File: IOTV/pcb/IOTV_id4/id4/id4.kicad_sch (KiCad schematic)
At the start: 7 parts, among them J1 Conn_01x04, J2 Conn_01x03, U1 WeMos_D1_mini

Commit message: pcb id4
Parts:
- removed D1, D2, D3, D4: LED, LED_THT:LED_D2.0mm_W4.8mm_H2.5mm_FlatTop, symbol Device:LED
- removed J1: Conn_01x04, Jumper:tht_jumper_x4-2.54mm, symbol PCM_4ms_Connector:Conn_01x04
- removed J2: Conn_01x03, Jumper:tht_jumper_x3-2.54mm, symbol PCM_4ms_Connector:Conn_01x03
- removed U1: WeMos_D1_mini, Module:WEMOS_D1_mini_light, symbol MCU_Module:WeMos_D1_mini
- added D1: LED_BGRK, symbol Device:LED_BGRK
- added Q1, Q2, Q3: S8050, Package_TO_SOT_THT:TO-92_Inline, symbol Transistor_BJT:S8050
- added R1, R2: 5, symbol Device:R
- added R3: 65, symbol Device:R
- added R4, R5, R6: 220, symbol Device:R
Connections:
- net GND: now also D1.4 (K)
- new net: Q1.2 (B), R4.2
- new net: Q1.1 (E), R1.1
- new net: D1.1 (BA), R1.2
- new net: Q3.1 (E), R2.1
- new net: D1.2 (GA), R2.2
- new net: Q3.2 (B), R5.2
- new net: Q2.1 (E), R3.1
- new net: D1.3 (RA), R3.2
- new net: Q2.2 (B), R6.2
- new net +3.3V: Q1.3 (C), Q2.3 (C), Q3.3 (C)
- new net GPIO_32: R4.1
- new net GPIO_33: R5.1
- new net GPIO_35: R6.1
- no-connect marks 9 -> 0

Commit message: pcb src id4
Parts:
- removed D1: LED_BGRK, symbol Device:LED_BGRK
- removed Q1, Q2, Q3: S8050, Package_TO_SOT_THT:TO-92_Inline, symbol Transistor_BJT:S8050
- removed R1, R2: 5, symbol Device:R
- removed R3: 65, symbol Device:R
- removed R4, R5, R6: 220, symbol Device:R
- added U1: ESP32-WROOM-32, RF_Module:ESP32-WROOM-32, symbol RF_Module:ESP32-WROOM-32
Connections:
- net GND: now also U1.1 (GND), U1.15 (GND), U1.38 (GND), U1.39 (GND)
- net GPIO_32: now also U1.8 (IO32)
- net GPIO_33: now also U1.9 (IO33)
- new net GPIO_12: U1.14 (IO12)
- new net GPIO_13: U1.16 (IO13)
- new net GPIO_14: U1.13 (IO14)
- new net GPIO_23: U1.37 (IO23)
- new net GPIO_25: U1.10 (IO25)
- new net GPIO_26: U1.11 (IO26)
- new net GPIO_27: U1.12 (IO27)
- new net VCC_3.3: U1.2 (VDD)
- no-connect marks 0 -> 24
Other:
- added sheet LEDS (untitled.kicad_sch)

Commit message: id4
pcd docs MK
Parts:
- added S1, S2, S3, S4: S-make-push, symbol PCM_Elektuur:S-make-push
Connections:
- net GND: now also S1.3, S2.3, S3.3, S4.3
- net GPIO_15: now reaches U1.23 (IO15)
- net GPIO_2: now reaches U1.24 (IO2)
- net GPIO_4: now reaches U1.26 (IO4)
- net GPIO_16: now reaches U1.27 (IO16)
- net GPIO_17: now reaches U1.28 (IO17)
- net GPIO_5: now reaches U1.29 (IO5)
- net GPIO_18: now reaches U1.30 (IO18)
- net GPIO_19: now reaches U1.31 (IO19)
- net GPIO_21: now reaches U1.33 (IO21)
- net GPIO_22: now reaches U1.36 (IO22)
- net GPIO_25: no longer names the net of U1.10 (IO25)
- net GPIO_26: no longer names the net of U1.11 (IO26)
- net GPIO_32: no longer names the net of U1.8 (IO32)
- net GPIO_33: no longer names the net of U1.9 (IO33)
- new net GPIO_34: S3.4
- new net GPIO_35: S4.4
- new net GPIO_36: S1.4
- new net GPIO_39: S2.4
- no-connect marks 24 -> 19

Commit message: pcb id4
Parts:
- removed S1, S2, S3, S4: S-make-push, symbol PCM_Elektuur:S-make-push
- removed U1: ESP32-WROOM-32, RF_Module:ESP32-WROOM-32, symbol RF_Module:ESP32-WROOM-32
- added SW1, SW2, SW3: SW_Push, Button_Switch_SMD:SW_SPST_TL3342, symbol Switch:SW_Push
- added U1: ESP32_DevKit_V1_DOIT, kicad:esp32_devkit_v1_doit, symbol esp32_devkit_v1_doit:ESP32_DevKit_V1_DOIT
- added U2: DFR0299, import:MODULE_DFR0299, symbol DFR0299:DFR0299
- added dynamic1: Speaker, Jumper:SolderJumper-2_P1.3mm_Open_Pad1.0x1.5mm, symbol Device:Speaker
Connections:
- net GND: now also U1.14 (GND), U1.17 (GND), U2.10 (GND), U2.7 (GND)
- net GPIO_12: now also U1.12 (IO12)
- net GPIO_13: now also U1.13 (IO13)
- net GPIO_14: now also U1.11 (IO14)
- net GPIO_15: now also U1.18 (IO15)
- net GPIO_16: now also U1.21 (IO16), U2.3 (TX)
- net GPIO_17: now also U1.22 (IO17), U2.2 (RX)
- net GPIO_18: now also U1.24 (IO18)
- net GPIO_19: now also U1.25 (IO19)
- net GPIO_2: now also U1.19 (IO2)
- net GPIO_21: now also U1.26 (IO21)
- net GPIO_22: now also U1.29 (IO22)
- net GPIO_23: now also U1.30 (IO23)
- net GPIO_27: now also U1.10 (IO27)
- net GPIO_34: now also SW3.2, U1.4 (IO34)
- net GPIO_35: now also SW1.2, U1.5 (IO35)
- net GPIO_36: now also U1.2 (SENSOR_VP), U2.16 (BUSY)
- net GPIO_39: now also SW2.2, U1.3 (SENSOR_VN)
- net GPIO_4: now also U1.20 (IO4)
- net GPIO_5: now also U1.23 (IO5)
- new net: U2.6 (SPK1), dynamic1.1
- new net: U2.8 (SPK2), dynamic1.2
- new net GPIO_32: U1.6 (IO32)
- new net GPIO_33: U1.7 (IO33)
- new net VCC_5: SW1.1, SW2.1, SW3.1, U1.15 (VIN), U2.1 (VCC)
- no-connect marks 19 -> 14

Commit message: PCB - ID4
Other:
- removed sheet LEDS
- added sheet Leds (leds.kicad_sch)
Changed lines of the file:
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@@
     )
   )
-  (sheet (at 230.886 74.676) (size 31.75 52.07) (fields_autoplaced)
+  (sheet (at 208.28 20.828) (size 38.862 48.006) (fields_autoplaced)
     (stroke (width 0.1524) (type solid))
     (fill (color 0 0 0 0.0000))
-    (property "Sheetname" "LEDS" (at 230.886 73.9644 0)
+    (property "Sheetname" "Leds" (at 208.28 20.1164 0)
       (effects (font (size 1.27 1.27)) (justify left bottom))
     )
-    (property "Sheetfile" "untitled.kicad_sch" (at 230.886 127.3306 0)
+    (property "Sheetfile" "leds.kicad_sch" (at 208.28 69.4186 0)
       (effects (font (size 1.27 1.27)) (justify left top))
     )

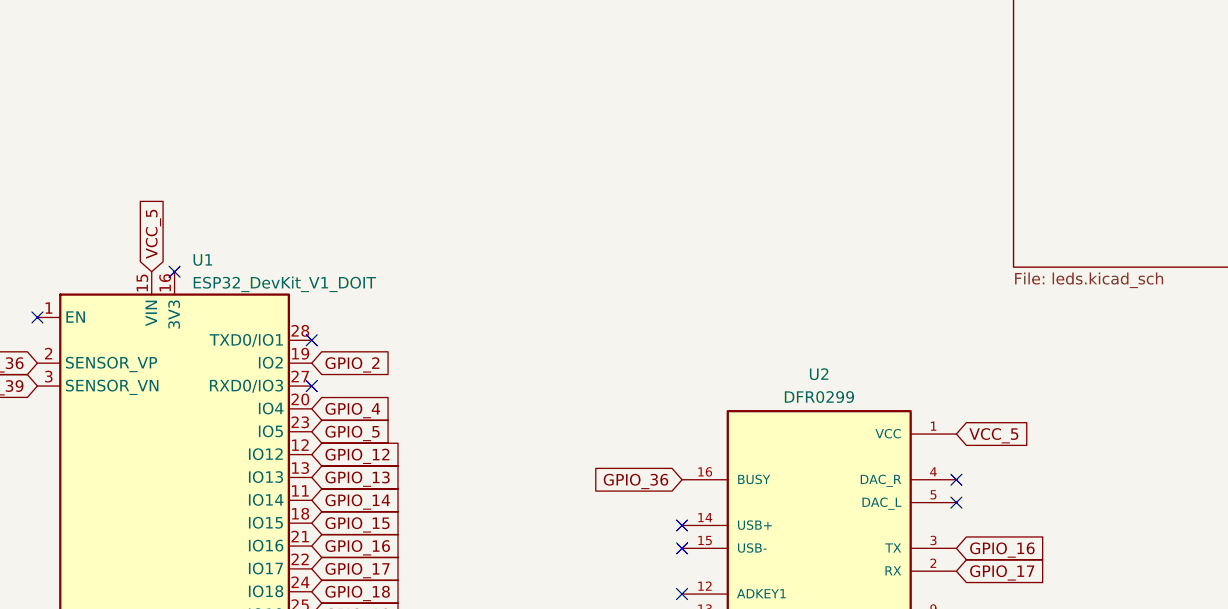
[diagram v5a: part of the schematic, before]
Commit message: pcb id4 - rezonit OK
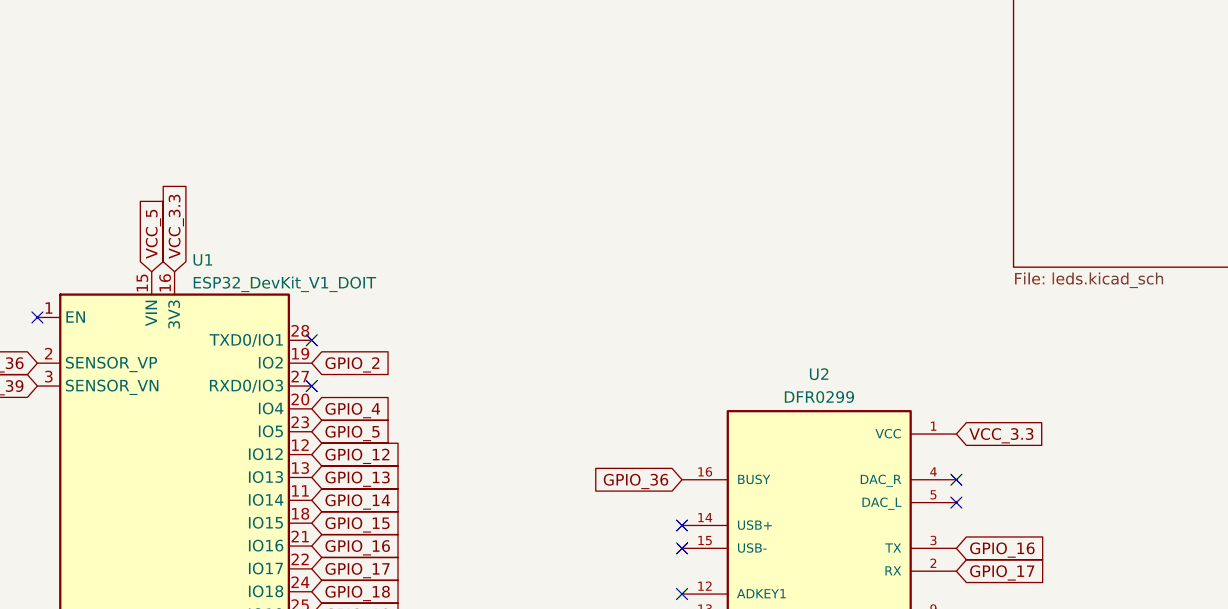
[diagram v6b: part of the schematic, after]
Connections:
- net VCC_5: no longer U2.1 (VCC)
- net VCC_3.3: now reaches U1.16 (3V3)
- net VCC_3.3: now also U2.1 (VCC)
- no-connect marks 14 -> 13
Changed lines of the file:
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@@
     (company "Вербкин М.С.")
   )
-  (no_connect (at 115.062 69.342))
   (no_connect (at 130.302 120.142))
   (no_connect (at 130.302 82.042))
@@
     )
   )
+  (global_label "VCC_3.3" (shape input) (at 201.93 87.376 0) (fields_autoplaced)
+    (effects (font (size 1.27 1.27)) (justify left))
+    (property "Intersheetrefs" "${INTERSHEET_REFS}" (at 212.4558 87.376 0)
+      (effects (font (size 1.27 1.27)) (justify left) hide)
+    )
+  )
   (global_label "VCC_5" (shape input) (at 112.522 69.342 90) (fields_autoplaced)
     (effects (font (size 1.27 1.27)) (justify left))
@@
     )
   )
-  (global_label "VCC_5" (shape input) (at 201.93 87.376 0) (fields_autoplaced)
-    (effects (font (size 1.27 1.27)) (justify left))
-    (property "Intersheetrefs" "${INTERSHEET_REFS}" (at 210.6415 87.376 0)
-      (effects (font (size 1.27 1.27)) (justify left) hide)
-    )
-  )
   (global_label "GND" (shape input) (at 35.56 107.696 0) (fields_autoplaced)
     (effects (font (size 1.27 1.27)) (justify left))
@@
       (effects (font (size 1.27 1.27)) (justify left) hide)
     )
+  )
+  (global_label "VCC_3.3" (shape input) (at 115.062 69.342 90) (fields_autoplaced)
+    (effects (font (size 1.27 1.27)) (justify left))
+    (property "Intersheetrefs" "${INTERSHEET_REFS}" (at 115.062 58.8162 90)
+      (effects (font (size 1.27 1.27)) (justify left) hide)
+    )

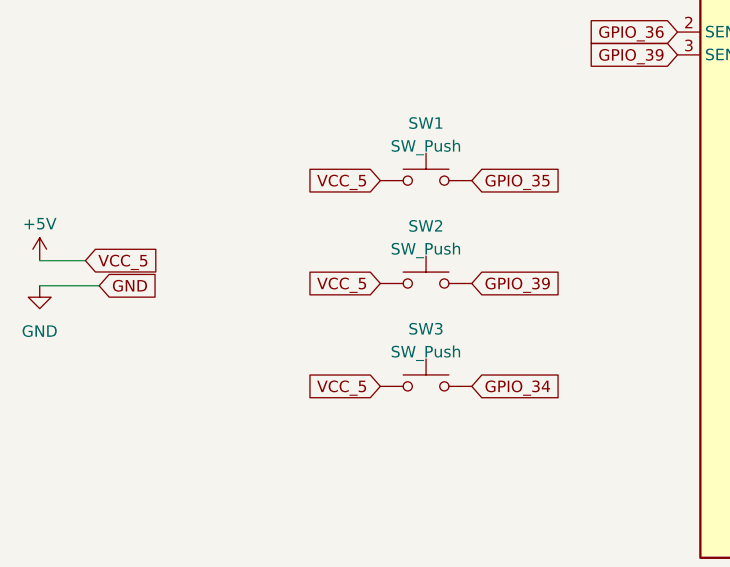
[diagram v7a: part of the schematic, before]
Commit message: pcd id 4
на кнопках исправлен контакт с 5в на 3,3в
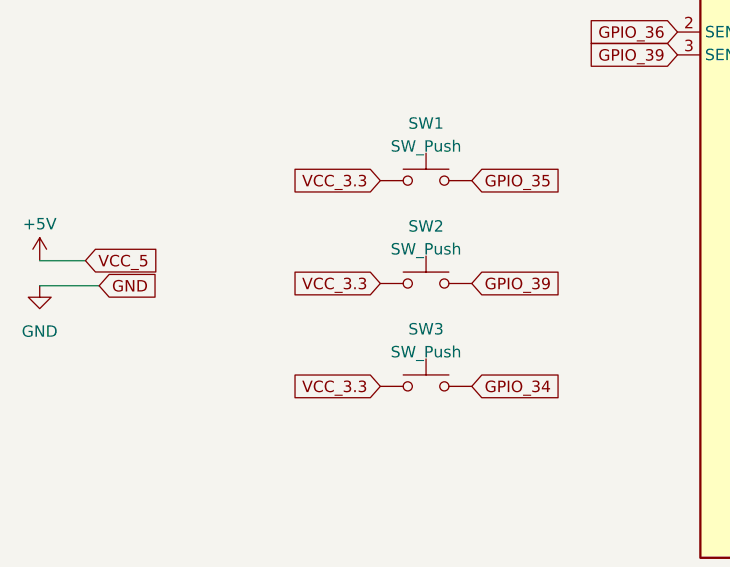
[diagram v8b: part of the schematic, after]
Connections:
- net VCC_3.3: now also SW1.1, SW2.1, SW3.1
- net VCC_5: no longer SW1.1, SW2.1, SW3.1
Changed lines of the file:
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@@
     )
   )
-  (global_label "VCC_5" (shape input) (at 66.802 96.012 180) (fields_autoplaced)
+  (global_label "VCC_3.3" (shape input) (at 66.802 96.012 180) (fields_autoplaced)
     (effects (font (size 1.27 1.27)) (justify right))
-    (property "Intersheetrefs" "${INTERSHEET_REFS}" (at 58.0905 96.012 0)
+    (property "Intersheetrefs" "${INTERSHEET_REFS}" (at 56.2762 96.012 0)
       (effects (font (size 1.27 1.27)) (justify right) hide)
     )
   )
-  (global_label "VCC_5" (shape input) (at 66.802 118.872 180) (fields_autoplaced)
+  (global_label "VCC_3.3" (shape input) (at 66.802 118.872 180) (fields_autoplaced)
     (effects (font (size 1.27 1.27)) (justify right))
-    (property "Intersheetrefs" "${INTERSHEET_REFS}" (at 58.0905 118.872 0)
+    (property "Intersheetrefs" "${INTERSHEET_REFS}" (at 56.2762 118.872 0)
       (effects (font (size 1.27 1.27)) (justify right) hide)
     )
@@
     )
   )
-  (global_label "VCC_5" (shape input) (at 66.802 107.442 180) (fields_autoplaced)
+  (global_label "VCC_3.3" (shape input) (at 66.802 107.442 180) (fields_autoplaced)
     (effects (font (size 1.27 1.27)) (justify right))
-    (property "Intersheetrefs" "${INTERSHEET_REFS}" (at 58.0905 107.442 0)
+    (property "Intersheetrefs" "${INTERSHEET_REFS}" (at 56.2762 107.442 0)
       (effects (font (size 1.27 1.27)) (justify right) hide)
     )
